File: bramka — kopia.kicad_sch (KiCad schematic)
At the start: 6 parts, among them Q5 NMOS, Q6 NMOS, Q7 NMOS, Q8 NMOS

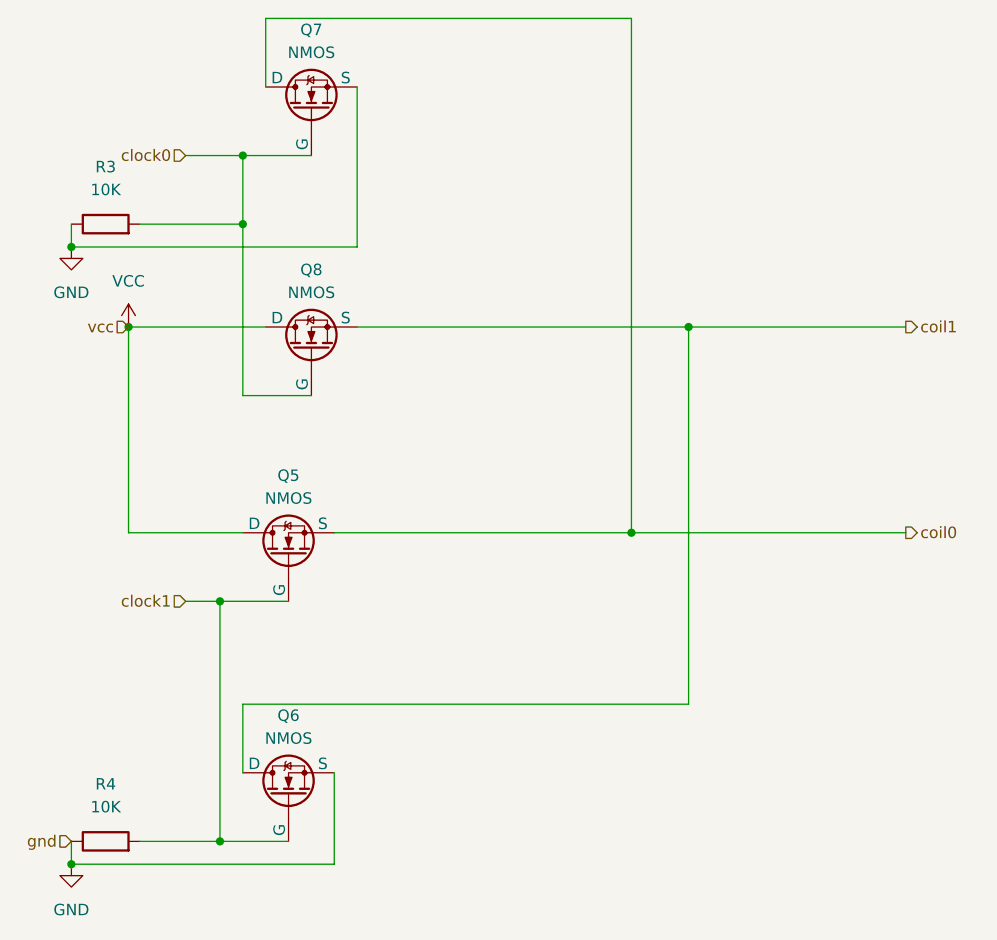
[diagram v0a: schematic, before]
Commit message: wojciechowe działania (poprawiono podschematy, dodano footprinty, pierwsze podejscie do pcb)
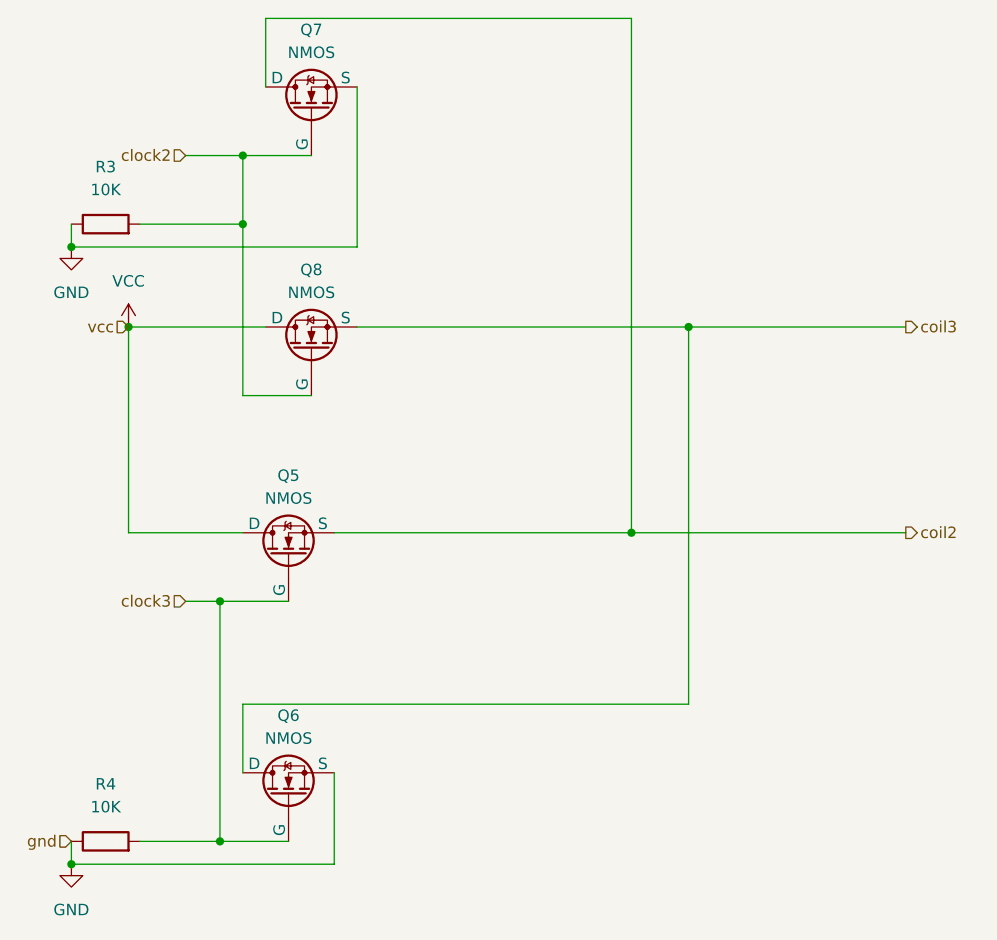
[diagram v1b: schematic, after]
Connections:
- net clock0 renamed clock2
- net clock1 renamed clock3
- net coil0 renamed coil2
- net coil1 renamed coil3
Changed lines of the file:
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@@
 		)
 	)
-	(hierarchical_label "coil1"
+	(hierarchical_label "coil3"
 		(shape output)
 		(at 157.48 80.01 0)
@@
 		)
 	)
-	(hierarchical_label "coil0"
+	(hierarchical_label "coil2"
 		(shape output)
 		(at 157.48 102.87 0)
@@
 		)
 	)
-	(hierarchical_label "clock1"
+	(hierarchical_label "clock3"
 		(shape input)
 		(at 77.47 110.49 180)
@@
 		)
 	)
-	(hierarchical_label "clock0"
+	(hierarchical_label "clock2"
 		(shape input)
 		(at 77.47 60.96 180)
